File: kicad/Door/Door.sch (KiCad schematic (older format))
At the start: 9 parts, among them Q1 Q_NMOS_GDS, Q2 Q_PMOS_GSD, SW1 SW_Push, U1 NODEMCU v3

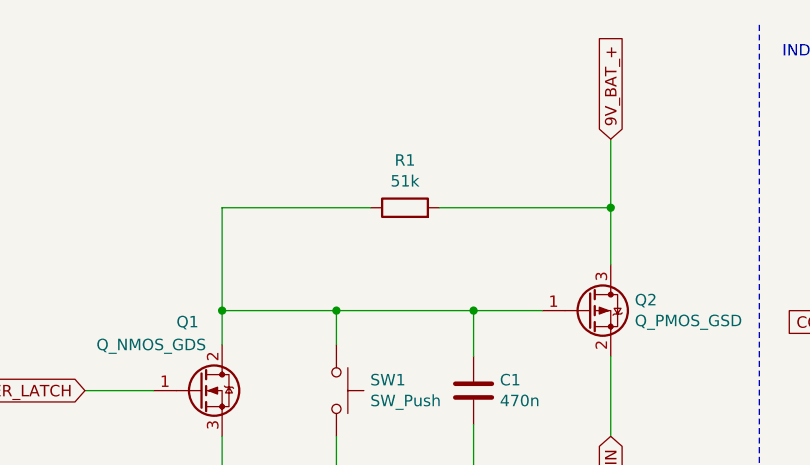
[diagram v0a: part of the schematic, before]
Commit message: PCB: Door: Set pull-up resistor to 200k to give ESP enough time to boot
Signed-off-by: CTXz <ctx.xda@gmail.com>
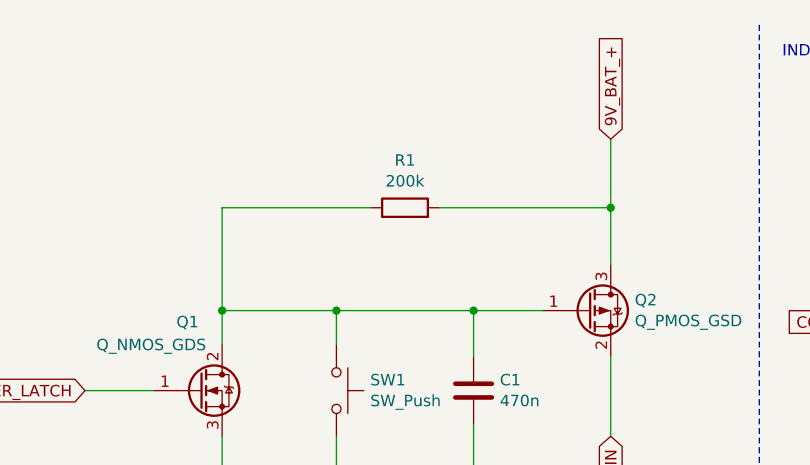
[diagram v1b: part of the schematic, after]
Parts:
- R1: value 51k -> 200k
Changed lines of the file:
@@
 P 3850 1300
 F 0 "R1" V 4057 1300 50  0000 C CNN
-F 1 "51k" V 3966 1300 50  0000 C CNN
+F 1 "200k" V 3966 1300 50  0000 C CNN
 F 2 "" V 3780 1300 50  0001 C CNN
 F 3 "~" H 3850 1300 50  0001 C CNN

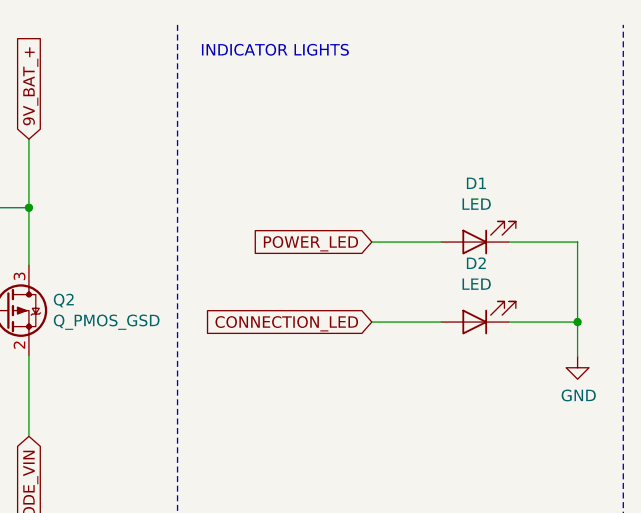
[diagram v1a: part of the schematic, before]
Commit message: PCB: Added PCB for Door board
Signed-off-by: CTXz <ctx.xda@gmail.com>
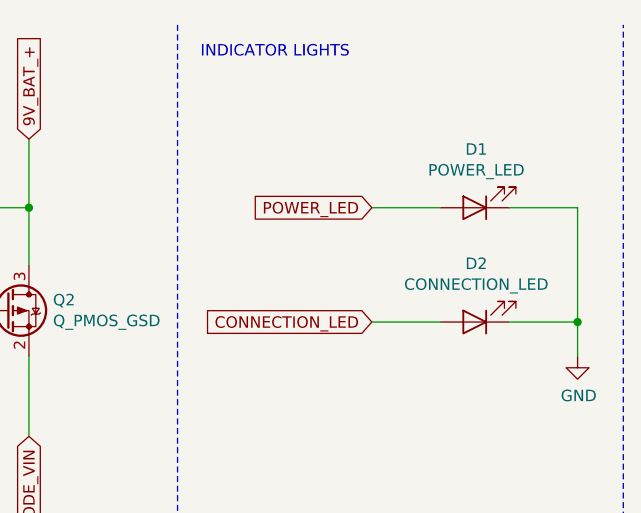
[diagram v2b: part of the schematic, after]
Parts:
- BT1, SW1: footprint (none) -> Connector_JST:JST_EH_B2B-EH-A_1x02_P2.50mm_Vertical
- C1: footprint (none) -> Capacitor_THT:C_Disc_D5.1mm_W3.2mm_P5.00mm
- D1: value LED -> POWER_LED; footprint (none) -> Connector_JST:JST_EH_B2B-EH-A_1x02_P2.50mm_Vertical
- D2: value LED -> CONNECTION_LED; footprint (none) -> Connector_JST:JST_EH_B2B-EH-A_1x02_P2.50mm_Vertical
- Q1, Q2: footprint (none) -> Package_TO_SOT_THT:TO-220-3_Horizontal_TabDown
- R1: footprint (none) -> Resistor_THT:R_Axial_DIN0207_L6.3mm_D2.5mm_P10.16mm_Horizontal
- U1: footprint MODULE_ZC563900 -> ZC563900_FP:MODULE_ZC563900
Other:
- moved on the sheet: D1
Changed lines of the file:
@@
 L Device:LED D1
 U 1 1 6188BE22
-P 6700 1450
-F 0 "D1" H 6693 1195 50  0000 C CNN
-F 1 "LED" H 6693 1286 50  0000 C CNN
-F 2 "" H 6700 1450 50  0001 C CNN
-F 3 "~" H 6700 1450 50  0001 C CNN
-	1    6700 1450
+P 6700 1300
+F 0 "D1" H 6693 1045 50  0000 C CNN
+F 1 "POWER_LED" H 6693 1136 50  0000 C CNN
+F 2 "Connector_JST:JST_EH_B2B-EH-A_1x02_P2.50mm_Vertical" H 6700 1300 50  0001 C CNN
+F 3 "~" H 6700 1300 50  0001 C CNN
+	1    6700 1300
 	-1   0    0    1
 $EndComp
@@
 F 0 "SW1" V 3504 2248 50  0000 L CNN
 F 1 "SW_Push" V 3595 2248 50  0000 L CNN
-F 2 "" H 3550 2300 50  0001 C CNN
+F 2 "Connector_JST:JST_EH_B2B-EH-A_1x02_P2.50mm_Vertical" H 3550 2300 50  0001 C CNN
 F 3 "~" H 3550 2300 50  0001 C CNN
 	1    3550 2100
@@
 F 0 "Q1" H 2850 2400 50  0000 L CNN
 F 1 "Q_NMOS_GDS" H 2500 2300 50  0000 L CNN
-F 2 "" H 3150 2200 50  0001 C CNN
+F 2 "Package_TO_SOT_THT:TO-220-3_Horizontal_TabDown" H 3150 2200 50  0001 C CNN
 F 3 "~" H 2950 2100 50  0001 C CNN
 	1    2950 2100
@@
 F 0 "Q2" H 4855 1796 50  0000 L CNN
 F 1 "Q_PMOS_GSD" H 4855 1705 50  0000 L CNN
-F 2 "" H 4850 1850 50  0001 C CNN
+F 2 "Package_TO_SOT_THT:TO-220-3_Horizontal_TabDown" H 4850 1850 50  0001 C CNN
 F 3 "~" H 4650 1750 50  0001 C CNN
 	1    4650 1750
@@
 F 0 "R1" V 4057 1300 50  0000 C CNN
 F 1 "200k" V 3966 1300 50  0000 C CNN
-F 2 "" V 3780 1300 50  0001 C CNN
+F 2 "Resistor_THT:R_Axial_DIN0207_L6.3mm_D2.5mm_P10.16mm_Horizontal" V 3780 1300 50  0001 C CNN
 F 3 "~" H 3850 1300 50  0001 C CNN
 	1    3850 1300
@@
 F 0 "C1" H 4265 2146 50  0000 L CNN
 F 1 "470n" H 4265 2055 50  0000 L CNN
-F 2 "" H 4188 1950 50  0001 C CNN
+F 2 "Capacitor_THT:C_Disc_D5.1mm_W3.2mm_P5.00mm" H 4188 1950 50  0001 C CNN
 F 3 "~" H 4150 2100 50  0001 C CNN
 	1    4150 2100
@@
 F 0 "U1" H 2100 5517 50  0000 C CNN
 F 1 "NODEMCU v3" H 2100 5426 50  0000 C CNN
-F 2 "MODULE_ZC563900" H 2100 4350 50  0001 L BNN
+F 2 "ZC563900_FP:MODULE_ZC563900" H 2100 4350 50  0001 L BNN
 F 3 "" H 2100 4350 50  0001 L BNN
 F 4 "N/A" H 2100 4350 50  0001 L BNN "MAXIMUM_PACKAGE_HEIGHT"
@@
 Wire Wire Line
 	3100 3650 2800 3650
-Text GLabel 6250 1450 0    50   Input ~ 0
+Text GLabel 6250 1300 0    50   Input ~ 0
 POWER_LED
 Wire Wire Line
-	6250 1450 6550 1450
+	6250 1300 6550 1300
 Text GLabel 6250 1800 0    50   Input ~ 0
 CONNECTION_LED
@@
 P 6700 1800
 F 0 "D2" H 6693 1545 50  0000 C CNN
-F 1 "LED" H 6693 1636 50  0000 C CNN
-F 2 "" H 6700 1800 50  0001 C CNN
+F 1 "CONNECTION_LED" H 6693 1636 50  0000 C CNN
+F 2 "Connector_JST:JST_EH_B2B-EH-A_1x02_P2.50mm_Vertical" H 6700 1800 50  0001 C CNN
 F 3 "~" H 6700 1800 50  0001 C CNN
 	1    6700 1800
@@
 	7150 1800 6850 1800
 Wire Wire Line
-	7150 1800 7150 1450
-Wire Wire Line
-	7150 1450 6850 1450
+	7150 1800 7150 1300
+Wire Wire Line
+	7150 1300 6850 1300
 Connection ~ 7150 1800
 Text GLabel 4750 1000 1    50   Input ~ 0
@@
 F 0 "BT1" H 1158 2096 50  0000 L CNN
 F 1 "Battery" H 1158 2005 50  0000 L CNN
-F 2 "" V 1050 2110 50  0001 C CNN
+F 2 "Connector_JST:JST_EH_B2B-EH-A_1x02_P2.50mm_Vertical" V 1050 2110 50  0001 C CNN
 F 3 "~" V 1050 2110 50  0001 C CNN
 	1    1050 2050

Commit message: Kicad: Finished 1st PCB revision
Signed-off-by: CTXz <ctx.xda@gmail.com>
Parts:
- added R2: 10k, Resistor_THT:R_Axial_DIN0207_L6.3mm_D2.5mm_P10.16mm_Horizontal, symbol Device:R
- added R3: 1k, Resistor_THT:R_Axial_DIN0207_L6.3mm_D2.5mm_P10.16mm_Horizontal, symbol Device:R
- added R4: 100, Resistor_THT:R_Axial_DIN0207_L6.3mm_D2.5mm_P10.16mm_Horizontal, symbol Device:R
- added SW2: USB/BAT, digikey-footprints:Toggle_Switch_100SP1T1B4M2QE, symbol Switch:SW_SPST
- added SW3: RST_BTN, Button_Switch_THT:SW_PUSH_6mm, symbol Switch:SW_Push
- D1: value POWER_LED -> POWER_LED (3mm RED)
- D2: value CONNECTION_LED -> CONNECTION_LED (3mm GREEN)
- U1: footprint ZC563900_FP:MODULE_ZC563900 -> ESP8266-Kicad:NodeMCU-LoLinV3
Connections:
- net labels added: DBG_BTN, RST_BTN
- wire segments 33 -> 41
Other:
- note added: "RESET BUTTON\nOptional for USB dev boards since SW1\nwon't work on USB supply. Alternatively\nthe NodeMCU's reset button can be used"
- moved on the sheet: D1, D2
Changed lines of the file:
@@
 Comment4 "Author: Patrick Pedersen"
 $EndDescr
-$Comp
-L Device:LED D1
-U 1 1 6188BE22
-P 6700 1300
-F 0 "D1" H 6693 1045 50  0000 C CNN
-F 1 "POWER_LED" H 6693 1136 50  0000 C CNN
-F 2 "Connector_JST:JST_EH_B2B-EH-A_1x02_P2.50mm_Vertical" H 6700 1300 50  0001 C CNN
-F 3 "~" H 6700 1300 50  0001 C CNN
-	1    6700 1300
-	-1   0    0    1
-$EndComp
-Wire Wire Line
-	3550 2600 3550 2450
-$Comp
-L power:GND #PWR03
-U 1 1 618BC0D4
-P 3550 2600
-F 0 "#PWR03" H 3550 2350 50  0001 C CNN
-F 1 "GND" H 3555 2427 50  0000 C CNN
-F 2 "" H 3550 2600 50  0001 C CNN
-F 3 "" H 3550 2600 50  0001 C CNN
-	1    3550 2600
-	1    0    0    -1
-$EndComp
 Wire Wire Line
 	3550 2450 4150 2450
 Connection ~ 3550 2450
 Wire Wire Line
-	3550 1750 4150 1750
-Connection ~ 3550 1750
-Wire Wire Line
 	3550 2300 3550 2450
 Wire Wire Line
@@
 Wire Wire Line
 	4150 1750 4450 1750
-Connection ~ 4150 1750
 Wire Wire Line
 	4150 1950 4150 1750
@@
 	3700 1300 3050 1300
 Wire Wire Line
-	3050 1300 3050 1750
-Wire Wire Line
 	3050 1750 3550 1750
 $Comp
@@
 Wire Wire Line
 	3050 1750 3050 1900
-Connection ~ 3050 1750
 Wire Wire Line
 	3050 2450 3050 2300
@@
 F 0 "U1" H 2100 5517 50  0000 C CNN
 F 1 "NODEMCU v3" H 2100 5426 50  0000 C CNN
-F 2 "ZC563900_FP:MODULE_ZC563900" H 2100 4350 50  0001 L BNN
+F 2 "ESP8266-Kicad:NodeMCU-LoLinV3" H 2100 4350 50  0001 L BNN
 F 3 "" H 2100 4350 50  0001 L BNN
 F 4 "N/A" H 2100 4350 50  0001 L BNN "MAXIMUM_PACKAGE_HEIGHT"
@@
 Wire Wire Line
 	3100 3650 2800 3650
-Text GLabel 6250 1300 0    50   Input ~ 0
+Text GLabel 6150 1300 0    50   Input ~ 0
 POWER_LED
 Wire Wire Line
-	6250 1300 6550 1300
-Text GLabel 6250 1800 0    50   Input ~ 0
+	6150 1300 6350 1300
+Text GLabel 6150 1800 0    50   Input ~ 0
 CONNECTION_LED
 $Comp
 L Device:LED D2
 U 1 1 6188BF54
-P 6700 1800
-F 0 "D2" H 6693 1545 50  0000 C CNN
-F 1 "CONNECTION_LED" H 6693 1636 50  0000 C CNN
-F 2 "Connector_JST:JST_EH_B2B-EH-A_1x02_P2.50mm_Vertical" H 6700 1800 50  0001 C CNN
-F 3 "~" H 6700 1800 50  0001 C CNN
-	1    6700 1800
+P 7150 1800
+F 0 "D2" H 7143 1545 50  0000 C CNN
+F 1 "CONNECTION_LED (3mm GREEN)" H 7143 1636 39  0000 C CNN
+F 2 "Connector_JST:JST_EH_B2B-EH-A_1x02_P2.50mm_Vertical" H 7150 1800 50  0001 C CNN
+F 3 "~" H 7150 1800 50  0001 C CNN
+	1    7150 1800
 	-1   0    0    1
 $EndComp
 Wire Wire Line
-	6250 1800 6550 1800
+	6150 1800 6350 1800
 $Comp
 L power:GND #PWR04
 U 1 1 618DE4C8
-P 7150 1950
-F 0 "#PWR04" H 7150 1700 50  0001 C CNN
-F 1 "GND" H 7155 1777 50  0000 C CNN
-F 2 "" H 7150 1950 50  0001 C CNN
-F 3 "" H 7150 1950 50  0001 C CNN
-	1    7150 1950
-	1    0    0    -1
-$EndComp
-Wire Wire Line
-	7150 1950 7150 1800
-Wire Wire Line
-	7150 1800 6850 1800
-Wire Wire Line
-	7150 1800 7150 1300
-Wire Wire Line
-	7150 1300 6850 1300
-Connection ~ 7150 1800
+P 7700 1950
+F 0 "#PWR04" H 7700 1700 50  0001 C CNN
+F 1 "GND" H 7705 1777 50  0000 C CNN
+F 2 "" H 7700 1950 50  0001 C CNN
+F 3 "" H 7700 1950 50  0001 C CNN
+	1    7700 1950
+	1    0    0    -1
+$EndComp
+Wire Wire Line
+	7700 1950 7700 1800
+Wire Wire Line
+	7700 1800 7300 1800
+Wire Wire Line
+	7700 1800 7700 1300
+Wire Wire Line
+	7700 1300 7300 1300
+Connection ~ 7700 1800
+Connection ~ 4750 1300
+Wire Notes Line
+	5400 500  5400 5550
+Text Notes 600  650  0    50   ~ 0
+POWER
+Text Notes 5500 650  0    50   ~ 0
+INDICATOR LIGHTS
+Text Notes 550  3150 0    50   ~ 0
+NODEMCU
+$Comp
+L Device:R R2
+U 1 1 61DA2B69
+P 6500 1300
+F 0 "R2" V 6707 1300 50  0000 C CNN
+F 1 "10k" V 6616 1300 50  0000 C CNN
+F 2 "Resistor_THT:R_Axial_DIN0207_L6.3mm_D2.5mm_P10.16mm_Horizontal" V 6430 1300 50  0001 C CNN
+F 3 "~" H 6500 1300 50  0001 C CNN
+	1    6500 1300
+	0    -1   -1   0
+$EndComp
+Wire Wire Line
+	6650 1300 7000 1300
+$Comp
+L Device:R R3
+U 1 1 61DA3210
+P 6500 1800
+F 0 "R3" V 6707 1800 50  0000 C CNN
+F 1 "1k" V 6616 1800 50  0000 C CNN
+F 2 "Resistor_THT:R_Axial_DIN0207_L6.3mm_D2.5mm_P10.16mm_Horizontal" V 6430 1800 50  0001 C CNN
+F 3 "~" H 6500 1800 50  0001 C CNN
+	1    6500 1800
+	0    -1   -1   0
+$EndComp
+Wire Wire Line
+	6650 1800 7000 1800
+$Comp
+L Device:LED D1
+U 1 1 6188BE22
+P 7150 1300
+F 0 "D1" H 7143 1045 50  0000 C CNN
+F 1 "POWER_LED (3mm RED)" H 7143 1136 39  0000 C CNN
+F 2 "Connector_JST:JST_EH_B2B-EH-A_1x02_P2.50mm_Vertical" H 7150 1300 50  0001 C CNN
+F 3 "~" H 7150 1300 50  0001 C CNN
+	1    7150 1300
+	-1   0    0    1
+$EndComp
+Wire Notes Line
+	500  2950 7850 2950
+Connection ~ 4150 1750
+Connection ~ 3550 1750
 Text GLabel 4750 1000 1    50   Input ~ 0
 9V_BAT_+
 Wire Wire Line
 	4750 1000 4750 1300
-Connection ~ 4750 1300
+Connection ~ 3050 1750
+Wire Wire Line
+	3050 1300 3050 1750
+$Comp
+L power:GND #PWR03
+U 1 1 618BC0D4
+P 3550 2600
+F 0 "#PWR03" H 3550 2350 50  0001 C CNN
+F 1 "GND" H 3555 2427 50  0000 C CNN
+F 2 "" H 3550 2600 50  0001 C CNN
+F 3 "" H 3550 2600 50  0001 C CNN
+	1    3550 2600
+	1    0    0    -1
+$EndComp
+Wire Wire Line
+	3550 2600 3550 2450
 $Comp
 L Device:Battery BT1
@@
 	1    0    0    -1
 $EndComp
-Text GLabel 1050 1700 1    50   Input ~ 0
-9V_BAT_+
-Wire Wire Line
-	1050 1700 1050 1850
+Connection ~ 1050 2400
+Wire Wire Line
+	1050 2250 1050 2400
+Wire Wire Line
+	1050 2400 1050 2450
 $Comp
 L power:GND #PWR01
@@
 $EndComp
 Wire Wire Line
-	1050 2250 1050 2400
-Connection ~ 1050 2400
-Wire Wire Line
-	1050 2400 1050 2450
-Wire Notes Line
-	7350 2950 7350 500
-Wire Notes Line
-	500  2950 7350 2950
-Wire Notes Line
-	5400 5550 500  5550
-Wire Notes Line
-	5400 500  5400 5550
-Text Notes 600  650  0    50   ~ 0
-POWER
-Text Notes 5500 650  0    50   ~ 0
-INDICATOR LIGHTS
-Text Notes 550  3150 0    50   ~ 0
-NODEMCU
+	3550 1750 3700 1750
+Wire Wire Line
+	4000 1750 4150 1750
+$Comp
+L Device:R R4
+U 1 1 61D70056
+P 3850 1750
+F 0 "R4" V 4057 1750 50  0000 C CNN
+F 1 "100" V 3966 1750 50  0000 C CNN
+F 2 "Resistor_THT:R_Axial_DIN0207_L6.3mm_D2.5mm_P10.16mm_Horizontal" V 3780 1750 50  0001 C CNN
+F 3 "~" H 3850 1750 50  0001 C CNN
+	1    3850 1750
+	0    -1   -1   0
+$EndComp
+Text GLabel 3100 3950 2    50   Input ~ 0
+DBG_BTN
+Wire Wire Line
+	3100 3950 2800 3950
+Text GLabel 1050 1150 1    50   Input ~ 0
+9V_BAT_+
+Wire Wire Line
+	1050 1150 1050 1300
+$Comp
+L Switch:SW_SPST SW2
+U 1 1 61DF5F15
+P 1050 1500
+F 0 "SW2" V 1004 1598 50  0000 L CNN
+F 1 "USB/BAT" V 1095 1598 50  0000 L CNN
+F 2 "digikey-footprints:Toggle_Switch_100SP1T1B4M2QE" H 1050 1500 50  0001 C CNN
+F 3 "~" H 1050 1500 50  0001 C CNN
+	1    1050 1500
+	0    1    1    0
+$EndComp
+Wire Wire Line
+	1050 1700 1050 1850
+Text GLabel 1100 3850 0    50   Input ~ 0
+RST_BTN
+Wire Wire Line
+	1100 3850 1400 3850
+$Comp
+L Switch:SW_Push SW3
+U 1 1 61E06F44
+P 6300 3850
+F 0 "SW3" H 6250 4050 50  0000 L CNN
+F 1 "RST_BTN" H 6250 4150 50  0000 L CNN
+F 2 "Button_Switch_THT:SW_PUSH_6mm" H 6300 4050 50  0001 C CNN
+F 3 "~" H 6300 4050 50  0001 C CNN
+	1    6300 3850
+	1    0    0    -1
+$EndComp
+Text GLabel 5950 3850 0    50   Input ~ 0
+RST_BTN
+Wire Wire Line
+	5950 3850 6100 3850
+$Comp
+L power:GND #PWR0101
+U 1 1 61E08EEB
+P 6650 3850
+F 0 "#PWR0101" H 6650 3600 50  0001 C CNN
+F 1 "GND" V 6500 3800 50  0000 C CNN
+F 2 "" H 6650 3850 50  0001 C CNN
+F 3 "" H 6650 3850 50  0001 C CNN
+	1    6650 3850
+	0    -1   -1   0
+$EndComp
+Wire Wire Line
+	6650 3850 6500 3850
+Text Notes 5500 3350 0    50   ~ 0
+RESET BUTTON\nOptional for USB dev boards since SW1\nwon't work on USB supply. Alternatively\nthe NodeMCU's reset button can be used
+Wire Notes Line
+	500  5550 5400 5550
+Wire Notes Line
+	5400 4150 7850 4150
+Wire Notes Line
+	7850 500  7850 4150
 $EndSCHEMATC
